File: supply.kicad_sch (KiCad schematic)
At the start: 10 parts, among them U2 AP62301WU-7

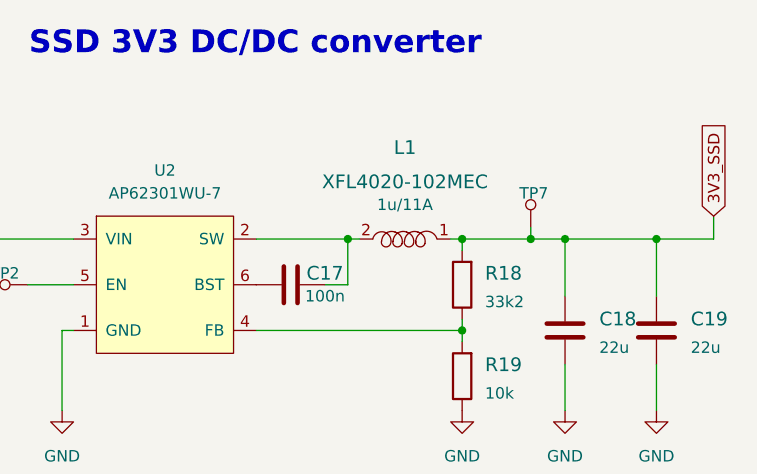
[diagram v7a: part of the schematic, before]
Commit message: Replaced 3.3V inductor with a smaller one to make m.2 fit
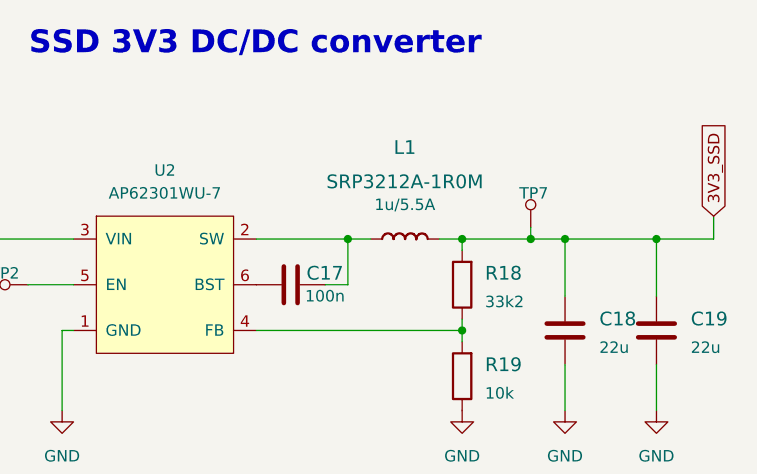
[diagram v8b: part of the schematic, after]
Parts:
- removed L1: XFL4020-102MEC, antmicro-footprints:XFL4020-102MEB, symbol antmicroFixedInductors:XFL4020-102MEC
- added L1: SRP3212A-1R0M, antmicro-footprints:SRP3212, symbol antmicroFixedInductors:SRP3212A-1R0M
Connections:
- net 3V3_SSD: now also L1.2 (P)
- net at C17.2, U2.2 (SW): now also L1.1 (P)
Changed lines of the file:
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@@
-    (stroke (width 0) (type default) (color 0 0 0 0))
-  )
-  (wire (pts (xy 215.9 142.24) (xy 217.17 142.24))
     (stroke (width 0) (type default) (color 0 0 0 0))
   )
@@
     (stroke (width 0) (type default) (color 0 0 0 0))
   )
+  (wire (pts (xy 226.06 142.24) (xy 228.6 142.24))
+    (stroke (width 0) (type default) (color 0 0 0 0))
+  )
   (wire (pts (xy 166.37 156.21) (xy 166.37 161.29))
     (stroke (width 0) (type default) (color 0 0 0 0))
@@
     (stroke (width 0) (type default) (color 0 0 0 0))
   )
-  (wire (pts (xy 227.33 142.24) (xy 228.6 142.24))
-    (stroke (width 0) (type default) (color 0 0 0 0))
-  )
   (wire (pts (xy 166.37 142.24) (xy 185.42 142.24))
     (stroke (width 0) (type default) (color 0 0 0 0))
@@
   )
   (wire (pts (xy 166.37 142.24) (xy 166.37 148.59))
+    (stroke (width 0) (type default) (color 0 0 0 0))
+  )
+  (wire (pts (xy 215.9 142.24) (xy 218.44 142.24))
     (stroke (width 0) (type default) (color 0 0 0 0))
   )
@@
     (pin "1")
   )
-  (symbol (lib_id "antmicroFixedInductors:XFL4020-102MEC") (at 222.25 142.24 180) (unit 1)
+  (symbol (lib_id "antmicroFixedInductors:SRP3212A-1R0M") (at 222.25 142.24 0) (unit 1)
     (in_bom yes) (on_board yes) (fields_autoplaced)
-    (property "Reference" "L1" (id 0) (at 222.25 132.08 0)
+    (property "Reference" "L1" (id 0) (at 222.2373 132.08 0)
       (effects (font (size 1.524 1.524)))
     )
-    (property "Value" "XFL4020-102MEC" (id 1) (at 222.25 135.89 0)
+    (property "Value" "SRP3212A-1R0M" (id 1) (at 222.2373 135.89 0)
       (effects (font (size 1.524 1.524)))
     )
-    (property "Footprint" "antmicro-footprints:XFL4020-102MEB" (id 2) (at 219.71 153.67 0)
-      (effects (font (size 1.524 1.524)) (justify left) hide)
-    )
-    (property "Datasheet" "" (id 3) (at 217.17 149.86 0)
-      (effects (font (size 1.524 1.524)) (justify left) hide)
-    )
-    (property "MPN" "XFL4020-102MEC" (id 4) (at 219.71 160.655 0)
-      (effects (font (size 1.524 1.524)) (justify left) hide)
-    )
-    (property "Manufacturer" "Coilcraft" (id 5) (at 219.71 163.195 0)
-      (effects (font (size 1.524 1.524)) (justify left) hide)
-    )
-    (property "MaxCur" "11A" (id 6) (at 217.805 158.115 0)
-      (effects (font (size 1.27 1.27)) hide)
-    )
-    (property "Size" "4.3x4.3" (id 7) (at 216.535 155.575 0)
-      (effects (font (size 1.27 1.27)) hide)
-    )
-    (property "Val" "1u/11A" (id 8) (at 222.25 138.43 0))
+    (property "Footprint" "antmicro-footprints:SRP3212" (id 2) (at 222.25 154.94 0)
+      (effects (font (size 1.524 1.524)) hide)
+    )
+    (property "Datasheet" "https://www.mouser.pl/datasheet/2/54/srp3212-2948733.pdf" (id 3) (at 222.25 154.94 0)
+      (effects (font (size 1.524 1.524)) hide)
+    )
+    (property "Manufacturer" "BOURNS" (id 4) (at 220.345 153.035 0)
+      (effects (font (size 1.27 1.27)) hide)
+    )
+    (property "MPN" "SRP3212A-1R0M" (id 5) (at 224.155 154.94 0)
+      (effects (font (size 1.27 1.27)) hide)
+    )
+    (property "MaxCur" "5.5A" (id 6) (at 219.075 158.75 0)
+      (effects (font (size 1.27 1.27)) hide)
+    )
+    (property "Size" "3.2x2.5" (id 7) (at 220.98 156.845 0)
+      (effects (font (size 1.27 1.27)) hide)
+    )
+    (property "Val" "1u/5.5A" (id 8) (at 222.2373 138.43 0))
     (pin "1")
     (pin "2")
